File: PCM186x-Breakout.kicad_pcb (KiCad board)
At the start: 2 copper layers, 38.1 x 17.8 mm, 15 parts, among them J1 Conn_01x15, J2 Conn_01x15

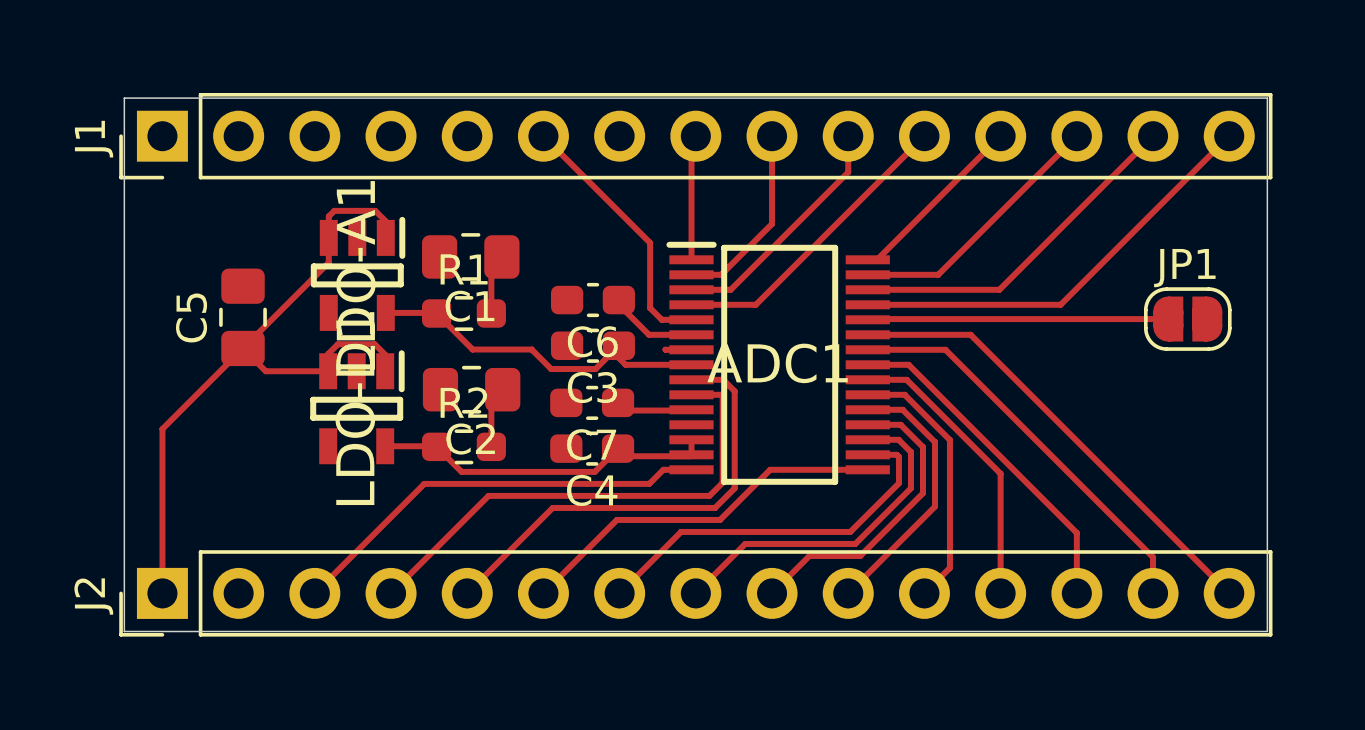
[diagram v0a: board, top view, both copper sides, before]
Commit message: addr pad, kicad 10, routing, silkscreen
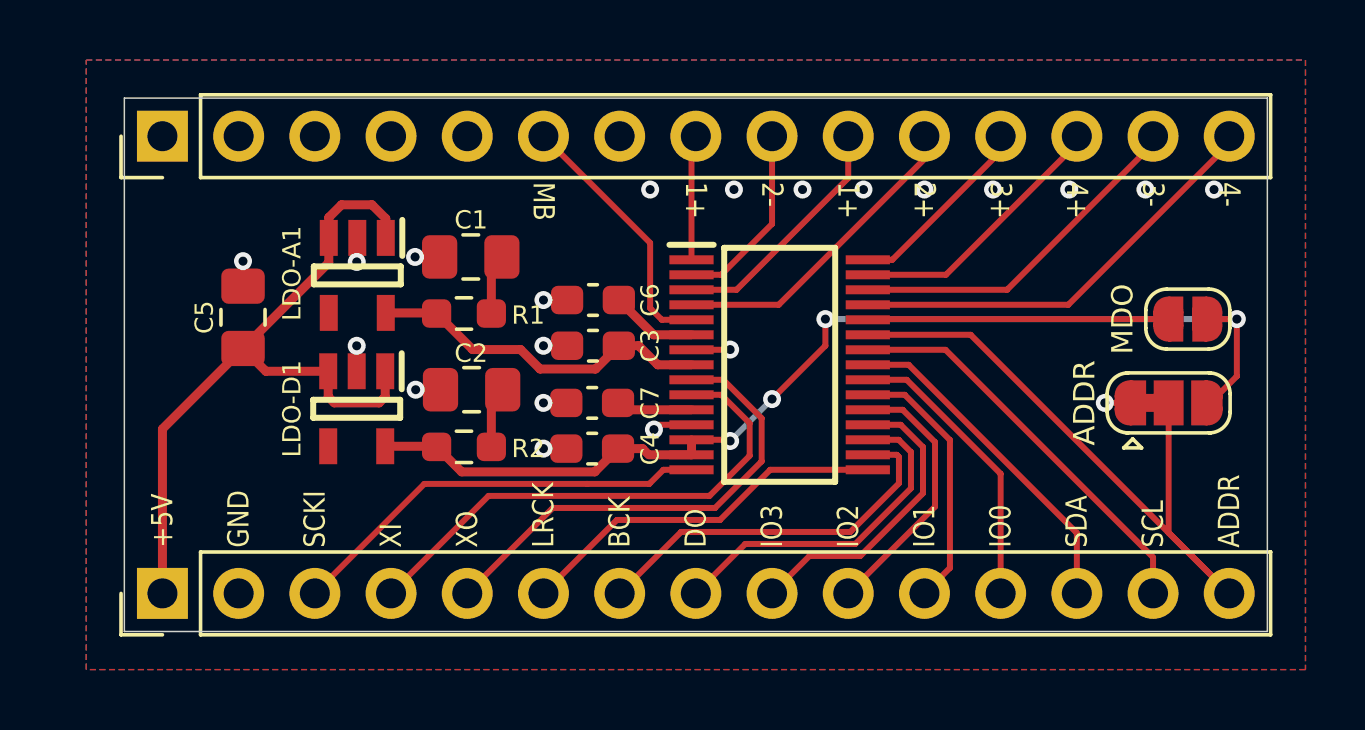
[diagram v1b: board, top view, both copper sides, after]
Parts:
- added JP2: SolderJumper_3_Bridged12, Jumper:SolderJumper-3_P1.3mm_Bridged12_RoundedPad1.0x1.5mm, F.Cu at (158.0, 59.7)
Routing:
- net VDD: track 11.5 -> 36.1 mm, vias 0 -> 4
- net GND: track 0.88 -> 10.7 mm, vias 0 -> 21
- net ADDR: track 15.6 -> 22.8 mm
- net XI: track 16.5 -> 17.3 mm
- net XO: track 15.2 -> 15.9 mm
- net +5V: track 24.0 -> 24.7 mm
- added copper zone on B.Cu, net GND
- added copper zone on F.Cu, net GND
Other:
- board text added: "+5V"
- board text added: "1+"
- board text added: "2+"
- board text added: "2-"
- board text added: "3+"
- board text added: "3-"
- board text added: "4+"
- board text added: "4-"
- board text added: "ADDR"
- board text added: "BCK"
- board text added: "DO"
- board text added: "GND"
- board text added: "IO0"
- board text added: "IO1"
- board text added: "IO2"
- board text added: "IO3"
- board text added: "LRCK"
- board text added: "MB"
- board text added: "MDO"
- board text added: "PCM186x Breakout Board"
- board text added: "SCKI"
- board text added: "SCL"
- board text added: "SDA"
- board text added: "XI"
- board text added: "XO"
- board text added: "r0 • Mar 2026 Cy Westbrook"

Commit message: make unused pins ground
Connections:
- J1 pad 1: unconnected-(J1-Pin_1-Pad1) -> GND
- J1 pad 2: unconnected-(J1-Pin_2-Pad2) -> GND
- J1 pad 3: unconnected-(J1-Pin_3-Pad3) -> GND
- J1 pad 4: unconnected-(J1-Pin_4-Pad4) -> GND
- J1 pad 5: unconnected-(J1-Pin_5-Pad5) -> GND
- J1 pad 7: unconnected-(J1-Pin_7-Pad7) -> GND
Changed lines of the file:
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@@
 			(layers "*.Cu" "*.Mask")
 			(remove_unused_layers no)
-			(net "unconnected-(J1-Pin_1-Pad1)")
+			(net "GND")
 			(pinfunction "Pin_1_1")
 			(pintype "passive")
@@
 			(layers "*.Cu" "*.Mask")
 			(remove_unused_layers no)
-			(net "unconnected-(J1-Pin_2-Pad2)")
+			(net "GND")
 			(pinfunction "Pin_2_2")
 			(pintype "passive")
@@
 			(layers "*.Cu" "*.Mask")
 			(remove_unused_layers no)
-			(net "unconnected-(J1-Pin_3-Pad3)")
+			(net "GND")
 			(pinfunction "Pin_3_3")
 			(pintype "passive")
@@
 			(layers "*.Cu" "*.Mask")
 			(remove_unused_layers no)
-			(net "unconnected-(J1-Pin_4-Pad4)")
+			(net "GND")
 			(pinfunction "Pin_4_4")
 			(pintype "passive")
@@
 			(layers "*.Cu" "*.Mask")
 			(remove_unused_layers no)
-			(net "unconnected-(J1-Pin_5-Pad5)")
+			(net "GND")
 			(pinfunction "Pin_5_5")
 			(pintype "passive")
@@
 			(layers "*.Cu" "*.Mask")
 			(remove_unused_layers no)
-			(net "unconnected-(J1-Pin_7-Pad7)")
+			(net "GND")
 			(pinfunction "Pin_7_7")
 			(pintype "passive")

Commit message: r0 final
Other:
- board text added: "G"
- board text added: "r0 • Mar 2026 • Cy Westbrook"
- board text removed: "r0 • Mar 2026 Cy Westbrook"
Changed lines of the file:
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@@
 		(tags "capacitor handsolder")
 		(property "Reference" "C1"
-			(at -0.009665 1.231171 0)
+			(at -2.422665 -0.038829 0)
 			(layer "F.SilkS")
 			(effects
@@
 		(start 123.19 49.53)
 		(end 161.29 67.31)
+		(radius 0.381)
 		(stroke
 			(width 0.05)
@@
 		)
 	)
+	(gr_text "G"
+		(at 124.46 52.324 270)
+		(layer "F.SilkS")
+		(effects
+			(font
+				(size 0.7112 0.6096)
+				(thickness 0.1524)
+			)
+			(justify left)
+		)
+	)
+	(gr_text "G"
+		(at 127 52.324 270)
+		(layer "F.SilkS")
+		(effects
+			(font
+				(size 0.7112 0.6096)
+				(thickness 0.1524)
+			)
+			(justify left)
+		)
+	)
+	(gr_text "G"
+		(at 129.54 52.324 270)
+		(layer "F.SilkS")
+		(effects
+			(font
+				(size 0.7112 0.6096)
+				(thickness 0.1524)
+			)
+			(justify left)
+		)
+	)
+	(gr_text "G"
+		(at 132.08 52.324 270)
+		(layer "F.SilkS")
+		(effects
+			(font
+				(size 0.7112 0.6096)
+				(thickness 0.1524)
+			)
+			(justify left)
+		)
+	)
+	(gr_text "G"
+		(at 134.62 52.324 270)
+		(layer "F.SilkS")
+		(effects
+			(font
+				(size 0.7112 0.6096)
+				(thickness 0.1524)
+			)
+			(justify left)
+		)
+	)
 	(gr_text "MB"
 		(at 137.16 52.324 270)
@@
 		)
 	)
+	(gr_text "G"
+		(at 139.7 52.324 270)
+		(layer "F.SilkS")
+		(effects
+			(font
+				(size 0.7112 0.6096)
+				(thickness 0.1524)
+			)
+			(justify left)
+		)
+	)
 	(gr_text "1+"
 		(at 142.24 52.324 270)
@@
 		)
 	)
-	(gr_text "r0 • Mar 2026\nCy Westbrook"
-		(at 156.972 60.452 0)
+	(gr_text "r0 • Mar 2026 • Cy Westbrook"
+		(at 142.24 59.182 0)
 		(layer "B.SilkS")
 		(effects
@@
 				(thickness 0.1778)
 			)
-			(justify left bottom mirror)
+			(justify top mirror)
 		)
 	)
 	(gr_text "PCM186x Breakout Board"
-		(at 156.972 57.404 0)
+		(at 142.24 58.42 0)
 		(layer "B.SilkS" knockout)
 		(effects
@@
 				(thickness 0.3048)
 			)
-			(justify left bottom mirror)
-		)
-	)
+			(justify bottom mirror)
+		)
+	)
